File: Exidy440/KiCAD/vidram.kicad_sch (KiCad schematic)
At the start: 35 parts, among them U10J 74LS74, U10K 74LS161, U10L 74LS32, U11J 74LS02, U11K 74LS161, U13K 74LS173, U13L 74LS157, U14K 74LS173, U14L MN2114, U15K 74LS374, U15L MN2114, U16K 74LS244, U16L MN2114, U17K 74LS245, U17L 74LS374, U18A 74LS189, U18K 74LS273, U18L 74LS273, U19A 74LS189, U20A 74LS189, U21A 74LS189, U22A 74LS169, U22F 74LS30, U22H 74LS283, U23C 74LS04, U23D 74LS08, U23F 74LS189, U23H 74LS283, U2L 74LS04, U5J 74LS04, U9K 74LS161

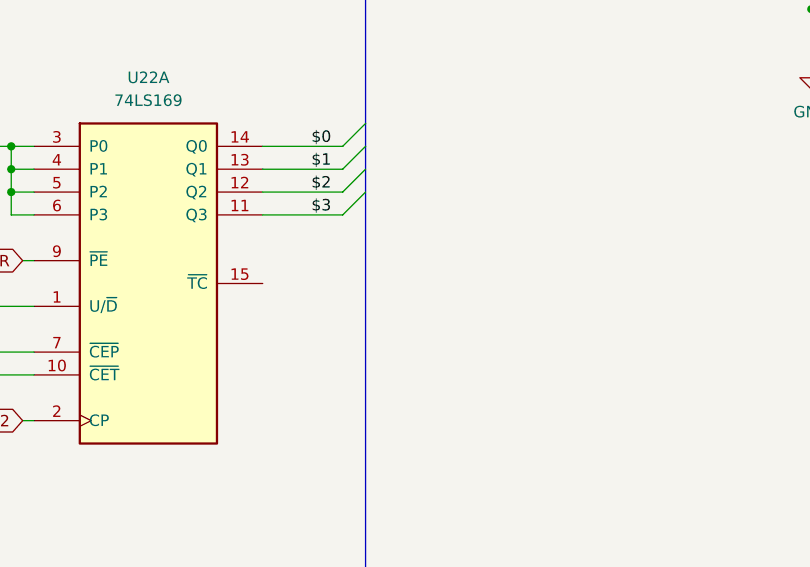
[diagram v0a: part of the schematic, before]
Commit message: Misc fixes found while checking clocks in FPGA core
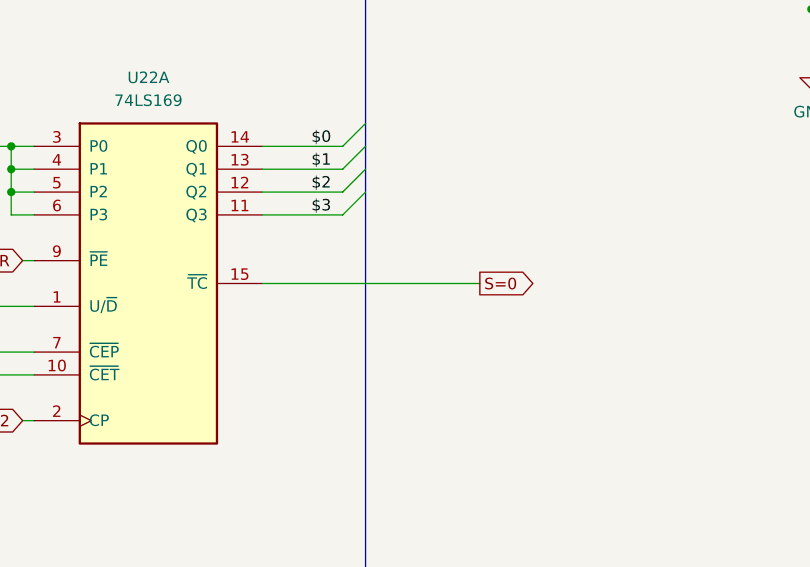
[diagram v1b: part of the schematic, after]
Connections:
- net S=0: now reaches U22A.15 (~{TC})
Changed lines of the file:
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@@
 	(wire
 		(pts
+			(xy 179.07 247.65) (xy 203.2 247.65)
+		)
+		(stroke
+			(width 0)
+			(type default)
+		)
+	)
+	(wire
+		(pts
 			(xy 166.37 138.43) (xy 163.83 138.43)
 		)
@@
 			)
 		)
+	)
+	(global_label "S=0"
+		(shape output)
+		(at 203.2 247.65 0)
+		(fields_autoplaced yes)
+		(effects
+			(font
+				(size 1.27 1.27)
+			)
+			(justify left)
+		)
+		(property "Intersheetrefs" "${INTERSHEET_REFS}"
+			(at 210.1766 247.65 0)
+			(effects
+				(font
+					(size 1.27 1.27)
+				)
+				(justify left)
+			)
+		)

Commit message: Added dual PCB structure, misc fixes and start of audio board IO
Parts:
- renumbered (4X) to (4X)?, U10J to U10J?, U10K to U10K?, U10L to U10L?, U11J to U11J?, U11K to U11K?, U13K to U13K?, U13L to U13L?, U14K to U14K?, U14L to U14L?, U15K to U15K?, U15L to U15L?, U16K to U16K?, U16L to U16L?, U17K to U17K?, U17L to U17L?, U18A to U18A?, U18K to U18K?, U18L to U18L?, U19A to U19A?, U20A to U20A?, U21A to U21A?, U22A to U22A?, U22F to U22F?, U22H to U22H?, U23C to U23C?, U23D to U23D?, U23F to U23F?, U23H to U23H?, U2L to U2L?, U5J to U5J?, U9K to U9K?

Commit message: Correction of references after copy/paste issue.  Additional IO on audio board.
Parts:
- gave numbers to parts that had none: 32

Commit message: Minor modifications to IO board
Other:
- moved on the sheet: U22A, U22FA, U22H, U23CF, U23DD, U23F, U23H
